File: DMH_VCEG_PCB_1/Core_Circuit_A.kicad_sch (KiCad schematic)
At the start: 87 parts, among them J23 Conn_01x10_PinHeader, J24 Conn_01x10_PinHeader, Q1 BC548, SW1 SW_DPDT_x2_On-Off-(On), SW2 SW_SPDT, SW3 SW_DPDT_x2, U1 TL074, U2 4001, U3 40106, U4 CD4066BE, U5 TL074, U6 4001, U7 TL074, U8 TL074

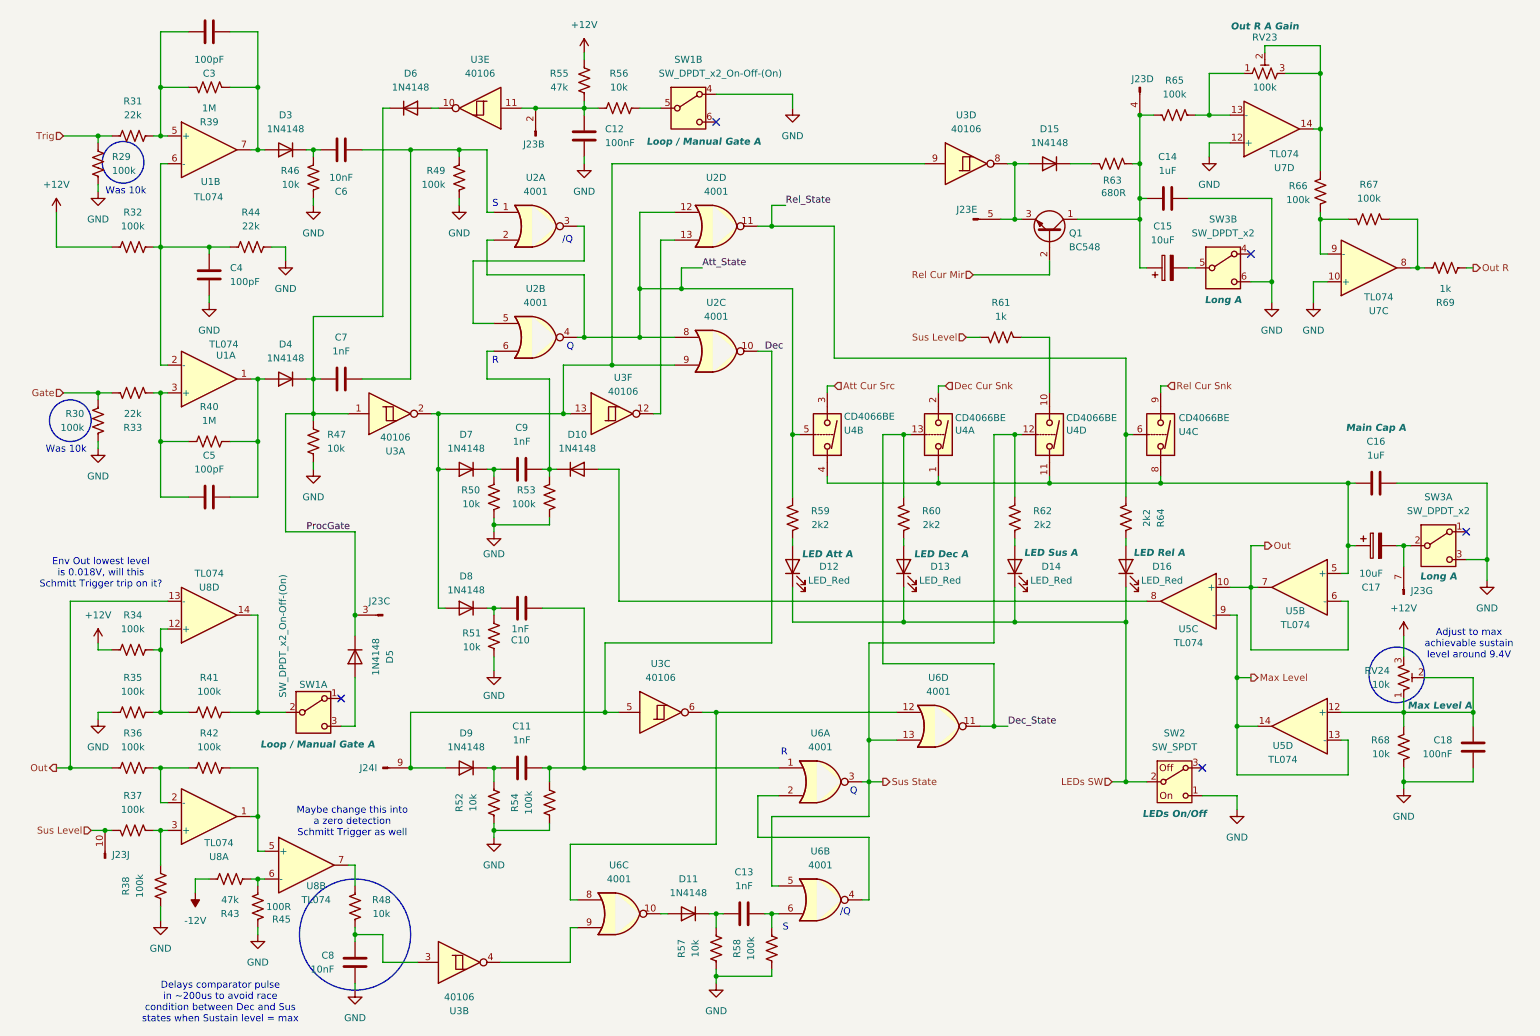
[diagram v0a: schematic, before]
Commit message: Divided components between PCB 1 and 2
Still need to:
- Place interface pins where needed
- Set "exclude from board" options where needed
- Copy schematic over to PCB 2 project
- Invert "exclude from board" options where needed
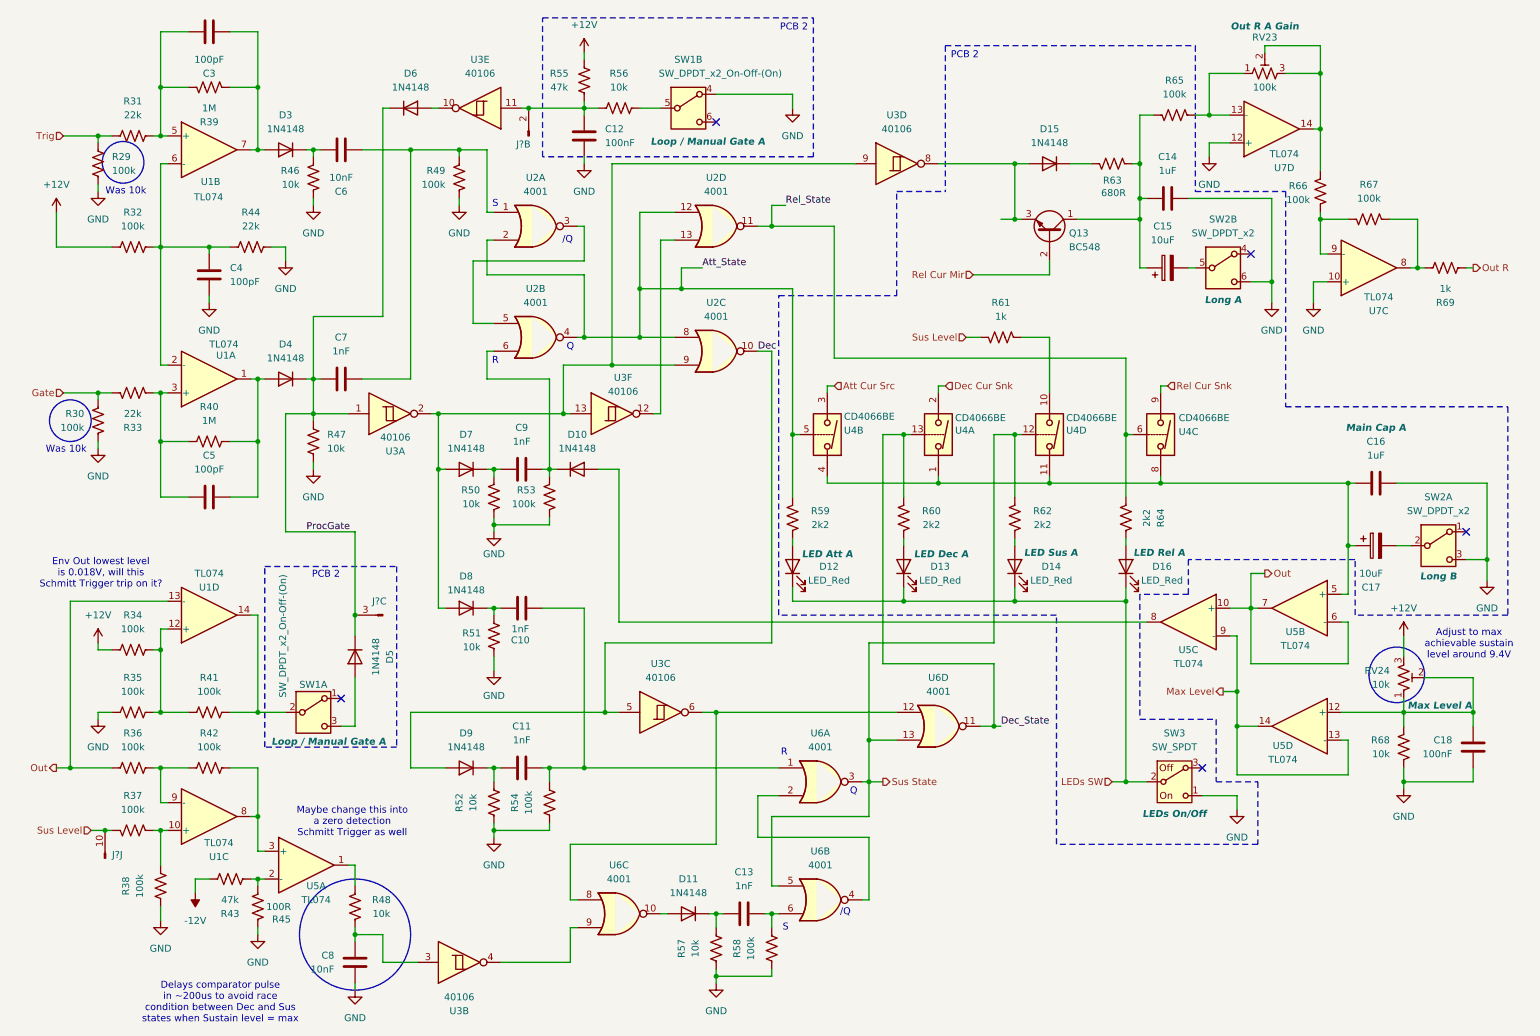
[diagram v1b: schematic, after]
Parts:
- removed unit 4 of J23
- removed unit 5 of J23
- removed unit 7 of J23
- removed J24: Conn_01x10_PinHeader, symbol SynthStuff:Conn_01x10_PinHeader
- SW2: renamed from SW3; Function Long A -> Long B
- renumbered J23 to J?, Q1 to Q13, SW3 to SW2, SW2 to SW3, U8 to U1, U8 to U5
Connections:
- net at R36.1, R42.2: now also U1.9 (-); no longer U1.2 (-)
- net at R37.2, R38.1: now also U1.10 (+); no longer U1.3 (+)
- net at R43.2, R45.1: now also U5.2 (-); no longer U5.6 (-)
- net at R48.1: now also U5.1; no longer U5.7
- new net: R42.1, U1.8, U5.3 (+)
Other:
- note added: "PCB 2"
- moved on the sheet: J?B, U3D, U5B, U5C

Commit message: Enhanced LED control in circuit A
Same on circuit B in progress
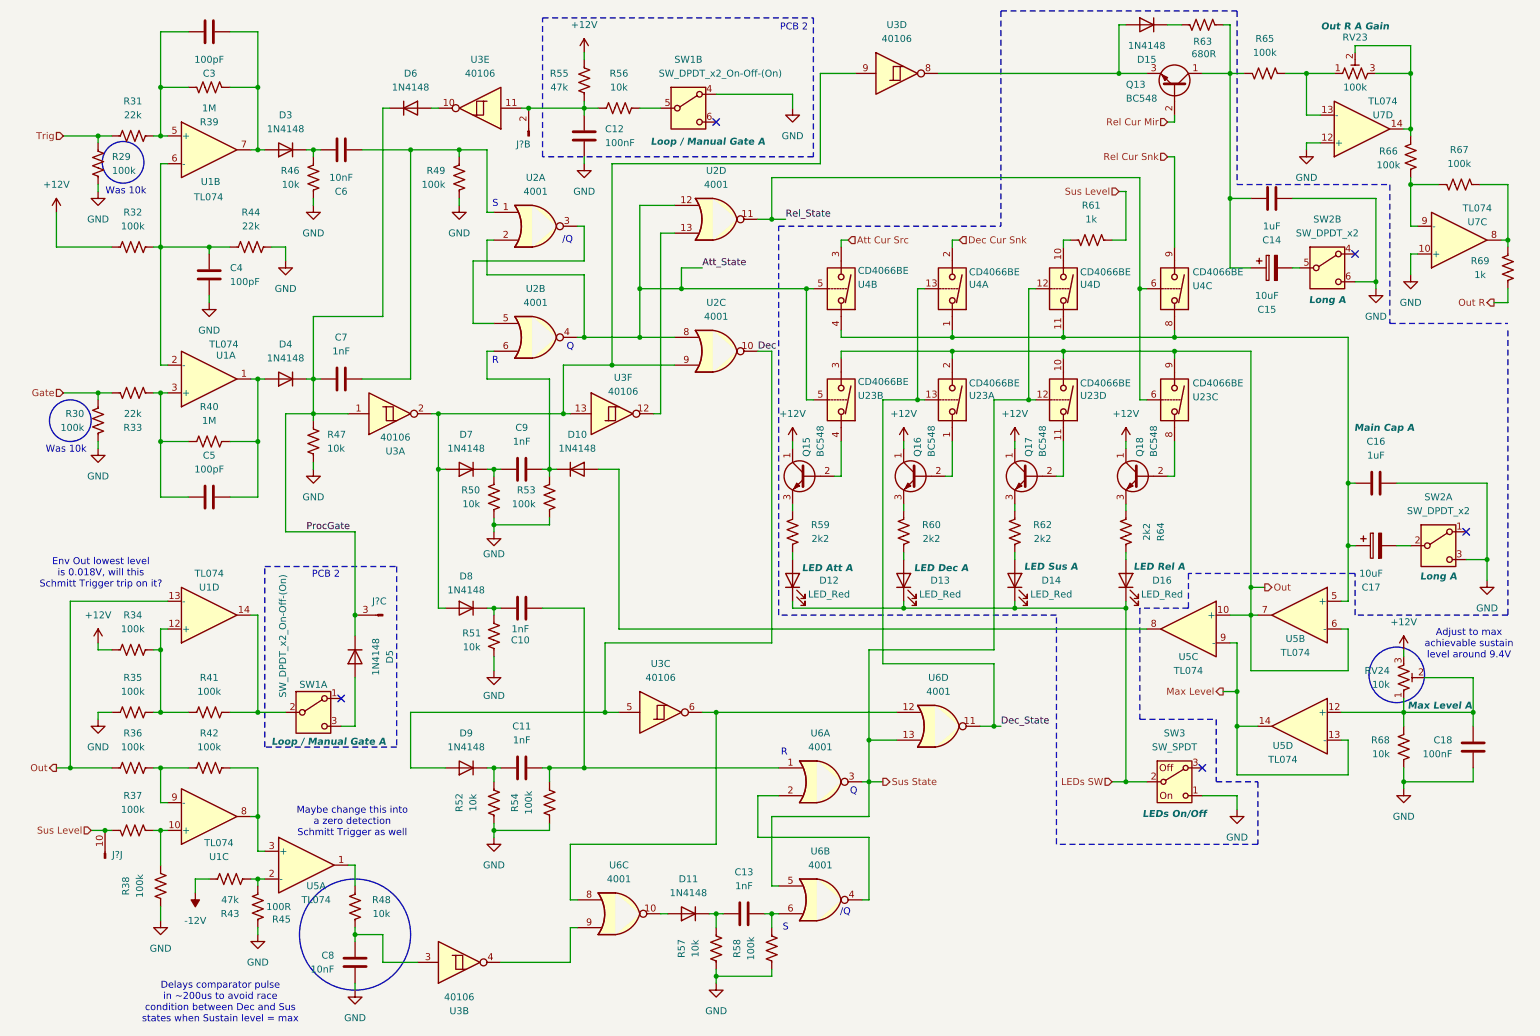
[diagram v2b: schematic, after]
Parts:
- added Q15, Q16, Q17, Q18: BC548, Package_TO_SOT_THT:TO-92L_Inline_Wide, symbol Transistor_BJT:BC548
- added U23: CD4066BE, Package_DIP:DIP-14_W7.62mm, symbol Analog_Switch:CD4066BE
- SW2: Function Long B -> Long A
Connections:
- net +12V: now also Q15.1 (C), Q16.1 (C), Q17.1 (C), Q18.1 (C)
- net Att_State: now also U23.5; no longer R59.1
- net Dec_State: now also U23.13; no longer R60.1
- net Out: now also U23.10, U23.2, U23.3, U23.9
- net Out R: now also R69.1; no longer R69.2
- net Rel_State: now also U23.6; no longer R64.1
- net Sus Level: now also R61.2; no longer R61.1
- net Sus State: now also U23.12; no longer R62.1
- net at U4.10: now also R61.1; no longer R61.2
- net at R67.2, U7.8: now also R69.2; no longer R69.1
- new net: Q17.2 (B), U23.11
- new net: Q17.3 (E), R62.1
- new net: Q18.2 (B), U23.8
- new net: Q18.3 (E), R64.1
- new net: Q15.3 (E), R59.1
- new net: Q16.2 (B), U23.1
- new net: Q15.2 (B), U23.4
- new net: Q16.3 (E), R60.1
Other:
- moved on the sheet: C14, C15, D12, D13, D14, D15, D16, Q13, R59, R60, R61, R62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

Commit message: Reworked Out R A circuit
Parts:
- removed D15: 1N4148, Diode_THT:D_DO-35_SOD27_P7.62mm_Horizontal, symbol Diode:1N4148
- removed Q13: BC548, Package_TO_SOT_THT:TO-92L_Inline_Wide, symbol Transistor_BJT:BC548
- removed R67: 100k, Resistor_THT:R_Axial_DIN0207_L6.3mm_D2.5mm_P7.62mm_Horizontal, symbol Device:R_US
- removed unit 4 of U3
- added Q13, Q19: BC558, Package_TO_SOT_THT:TO-92L_Inline_Wide, symbol Transistor_BJT:BC558
- added Q20, Q21: MMBFJ113, Package_TO_SOT_THT:TO-92L_Inline, symbol Transistor_FET:MMBFJ113
- added Q22, Q23: BC548, Package_TO_SOT_THT:TO-92L_Inline_Wide, symbol Transistor_BJT:BC548
- added R183, R185, R187, R188: 100k, Resistor_THT:R_Axial_DIN0207_L6.3mm_D2.5mm_P7.62mm_Horizontal, symbol Device:R_US
- added R184, R186: 4k7, Resistor_THT:R_Axial_DIN0207_L6.3mm_D2.5mm_P7.62mm_Horizontal, symbol Device:R_US
- added RV41: 50k, Potentiometer_THT:Potentiometer_Bourns_3296X_Horizontal, symbol Device:R_Potentiometer_Trim_US
- R63: value 680R -> 82k
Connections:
- net -12V: now also R187.1, RV41.1, RV41.2
- net GND: now also C14.1, Q23.3 (E), R183.2, R186.1; no longer C14.2, U7.10 (+)
- net ProcGate: now also C5.2, D4.2 (A), R40.1, R66.2, U1.1; no longer C7.1, D4.1 (K), D5.1 (K), D6.1 (K), J?.3 (Pin_3), R47.2, U3.1
- net at R65.2, RV23.1, U7.13 (-): now also R63.2
- net at RV23.2, RV23.3, U7.14: now also Q19.3 (E), R184.1; no longer R66.1
- net InvGate: now reaches D7.2 (A), D8.2 (A), U2.9, U3.13, U3.2
- net InvGate: now also R65.1, R188.2
- net at R69.2, U7.8: now also U7.9 (-)
- new net: Q21.3 (G), R187.2, R188.1
- new net: C14.2, C15.1, Q20.2 (S), Q21.2 (S), U7.10 (+)
- new net: C7.1, D4.1 (K), D5.1 (K), D6.1 (K), J?.3 (Pin_3), R47.2, U3.1
- new net: Q20.3 (G), R66.1
- new net: R63.1, RV41.3
- new net: Q21.1 (D), Q23.1 (C)
- new net: Q13.1 (C), Q13.2 (B), Q19.2 (B), R183.1
- new net: Q13.3 (E), R184.2
- new net: Q22.1 (C), Q22.2 (B), Q23.2 (B), R185.2
- new net: Q22.3 (E), R186.2
- new net: Q19.1 (C), Q20.1 (D)
- new net Rel Proc CV: R185.1
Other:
- moved on the sheet: C14, C15, C16, C17, R61, R65, R69, RV23, SW2A, SW2B, U7C

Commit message: Copied Circuit A into B
And added diode to protect input of U3B
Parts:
- added D15: 1N4148, Diode_THT:D_DO-35_SOD27_P7.62mm_Horizontal, symbol Diode:1N4148
- added R67: 10k, Resistor_THT:R_Axial_DIN0207_L6.3mm_D2.5mm_P7.62mm_Horizontal, symbol Device:R_US
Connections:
- net GND: now also R67.2
- net at U5.1: now also D15.2 (A); no longer R48.1
- new net: D15.1 (K), R48.1, R67.1
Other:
- note removed: "Env Out lowest level is 0.018V, will this Schmitt Trigger trip on it?"
- note removed: "Maybe change this into a zero detection Schmitt Trigger as well"
- moved on the sheet: C10, C11, C12, C13, C14, C15, C16, C17, C18, C3, C4, C5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

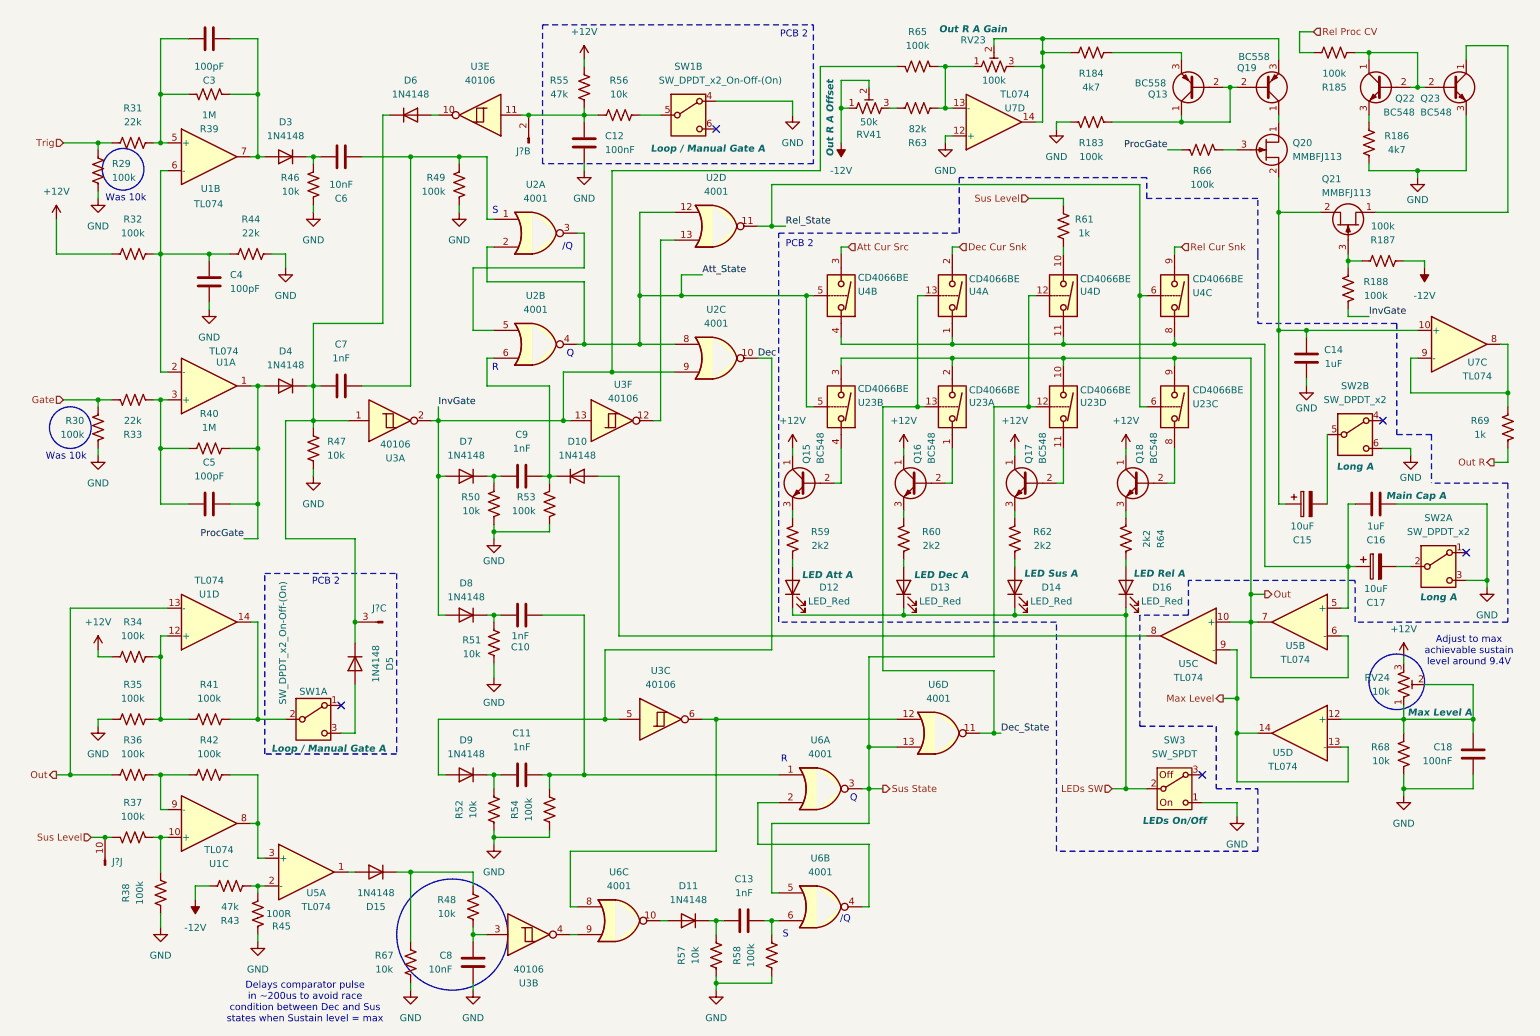
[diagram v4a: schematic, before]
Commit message: Re-annotated whole circuit
Now need to place interface pins and determine in and out of board settings
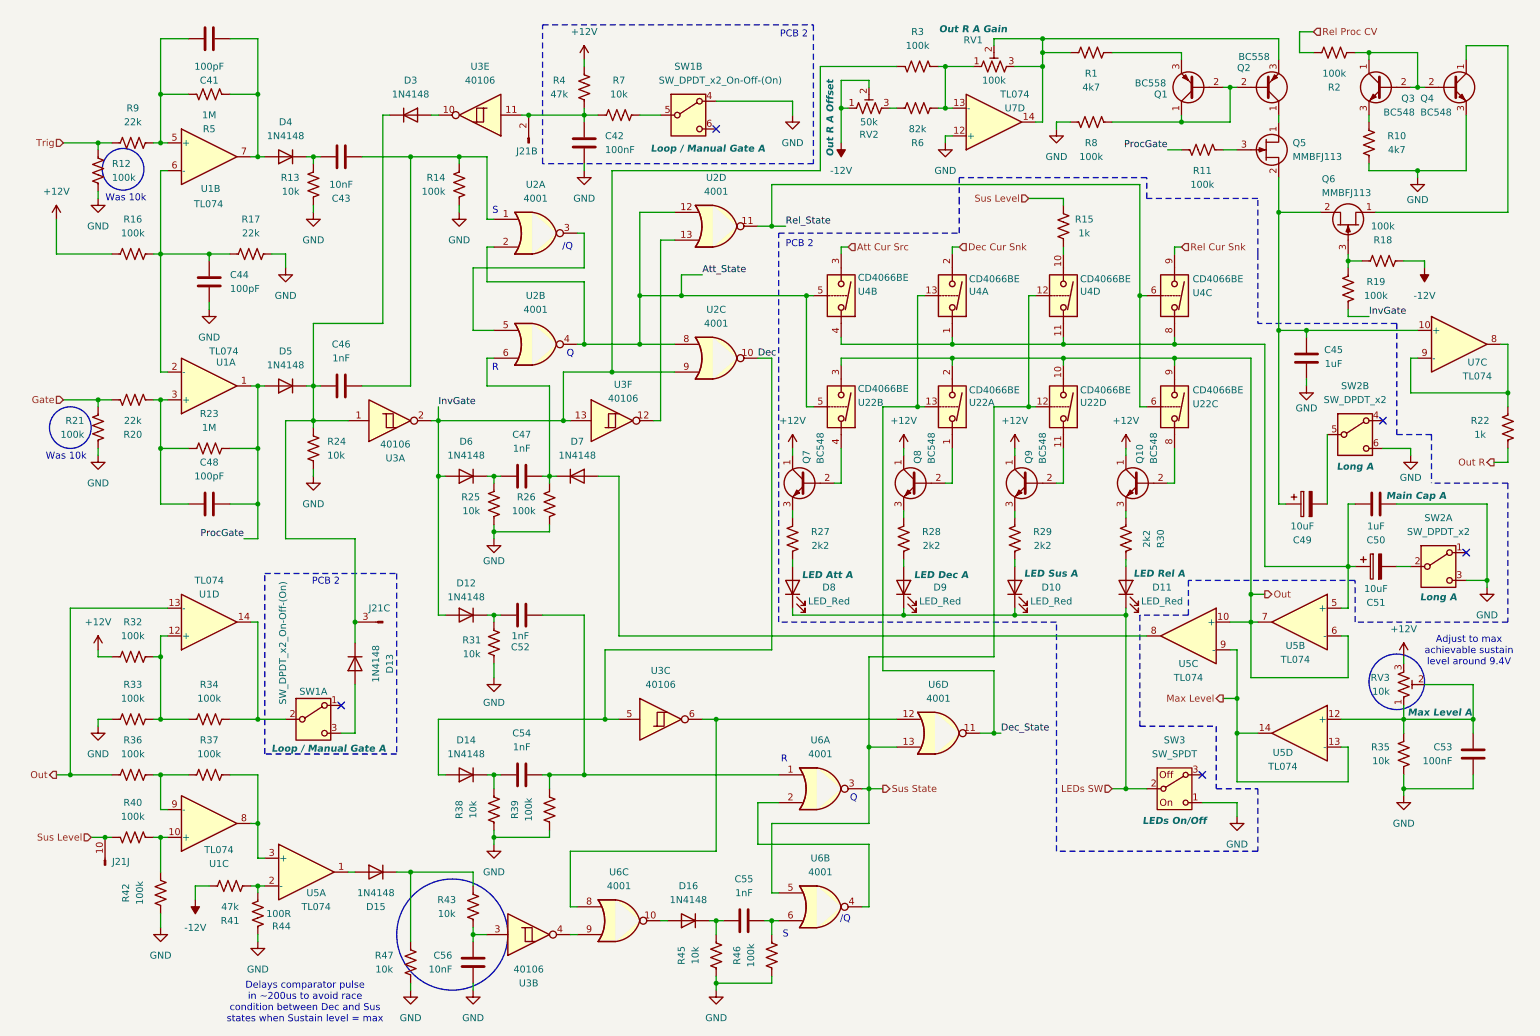
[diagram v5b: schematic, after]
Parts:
- gave numbers to parts that had none: 1
- renumbered C3 to C41, C12 to C42, C6 to C43, C4 to C44, C14 to C45, C7 to C46, C9 to C47, C5 to C48, C15 to C49, C16 to C50, C17 to C51, C10 to C52, C18 to C53, C11 to C54, C13 to C55, C8 to C56, D14 to D10, D16 to D11, D8 to D12, D5 to D13, D9 to D14, D11 to D16, D6 to D3, D3 to D4, D4 to D5, D7 to D6, D10 to D7, D12 to D8, D13 to D9, Q13 to Q1, Q18 to Q10, Q19 to Q2, Q22 to Q3, Q23 to Q4, Q20 to Q5, Q21 to Q6, Q15 to Q7, Q16 to Q8, Q17 to Q9, R184 to R1, R186 to R10, R66 to R11, R29 to R12, R46 to R13, R49 to R14, R61 to R15, R32 to R16, R44 to R17, R187 to R18, R188 to R19, R185 to R2, R33 to R20, R30 to R21, R69 to R22, R40 to R23, R47 to R24, R50 to R25, R53 to R26, R59 to R27, R60 to R28, R62 to R29, R65 to R3, R64 to R30, R51 to R31, R34 to R32, R35 to R33, R41 to R34, R68 to R35, R42 to R37, R52 to R38, R54 to R39, R55 to R4, R37 to R40, R43 to R41, R38 to R42, R48 to R43, R45 to R44, R57 to R45, R58 to R46, R67 to R47, R39 to R5, R63 to R6, R56 to R7, R183 to R8, R31 to R9, RV23 to RV1, RV41 to RV2, RV24 to RV3, U23 to U22

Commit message: Ready for breadboarding
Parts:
- added unit 7 of J21
- added unit 2 of J21
- added unit 5 of J21
- added unit 8 of J21
- added unit 3 of J21
- added unit 4 of J21
- added unit 6 of J21
- added unit 9 of J22
- added unit 3 of J24
- C45, C50: footprint Capacitor_THT:C_Disc_D4.3mm_W1.9mm_P5.00mm -> Capacitor_THT:C_Rect_L7.0mm_W4.5mm_P5.00mm
- C49, C51: footprint Capacitor_THT:CP_Radial_D5.0mm_P2.00mm -> Capacitor_THT:CP_Radial_D4.0mm_P1.50mm
- J22: renamed from J21; footprint (none) -> Connector_PinHeader_2.54mm:PinHeader_1x10_P2.54mm_Vertical
- J24: renamed from J21; value Conn_01x10_PinHeader -> Conn_01x06_PinHeader; footprint (none) -> Connector_PinHeader_2.54mm:PinHeader_1x06_P2.54mm_Vertical; symbol SynthStuff:Conn_01x10_PinHeader -> SynthStuff:Conn_01x06_PinHeader
- RV1, RV2: footprint Potentiometer_THT:Potentiometer_Bourns_3296X_Horizontal -> Potentiometer_THT:Potentiometer_Bourns_3296W_Vertical
- SW1: footprint (none) -> SynthStuff:Toggle_Switch_2_Poles_TE
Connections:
- net Att_State: now also J21.4 (Pin_4)
- net Dec_State: now also J21.2 (Pin_2)
- net Out: now also J21.8 (Pin_8)
- net Rel Proc CV: now also J22.9 (Pin_9)
- net Rel_State: now also J21.5 (Pin_5)
- net Sus State: now also J21.3 (Pin_3)
- net at C45.2, C49.1, Q5.2 (S)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: now also J21.6 (Pin_6)
- net at C42.1, R4.2, R7.2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: now also J21.9 (Pin_9); no longer J21.2 (Pin_2)
- net at C50.1, C51.1, U4.1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: now also J21.7 (Pin_7)
- net at C46.1, D13.1 (K), D3.1 (K)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: now also J24.2 (Pin_2); no longer J24.3 (Pin_3)
- net at R34.1, SW1.2 (B), U1.14: now also J24.3 (Pin_3)
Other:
- moved on the sheet: J24B, Q3, Q4, R10, R2
